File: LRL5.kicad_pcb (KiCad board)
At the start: 2 copper layers, 150 x 50 mm, 38 parts, among them J1 POWER, J2 On/Off, J5 OUT, J6 MODE, J7 ADJUST, Q1 BC549, U1 BA033CC0T, U2 NHD-C0220BIZ

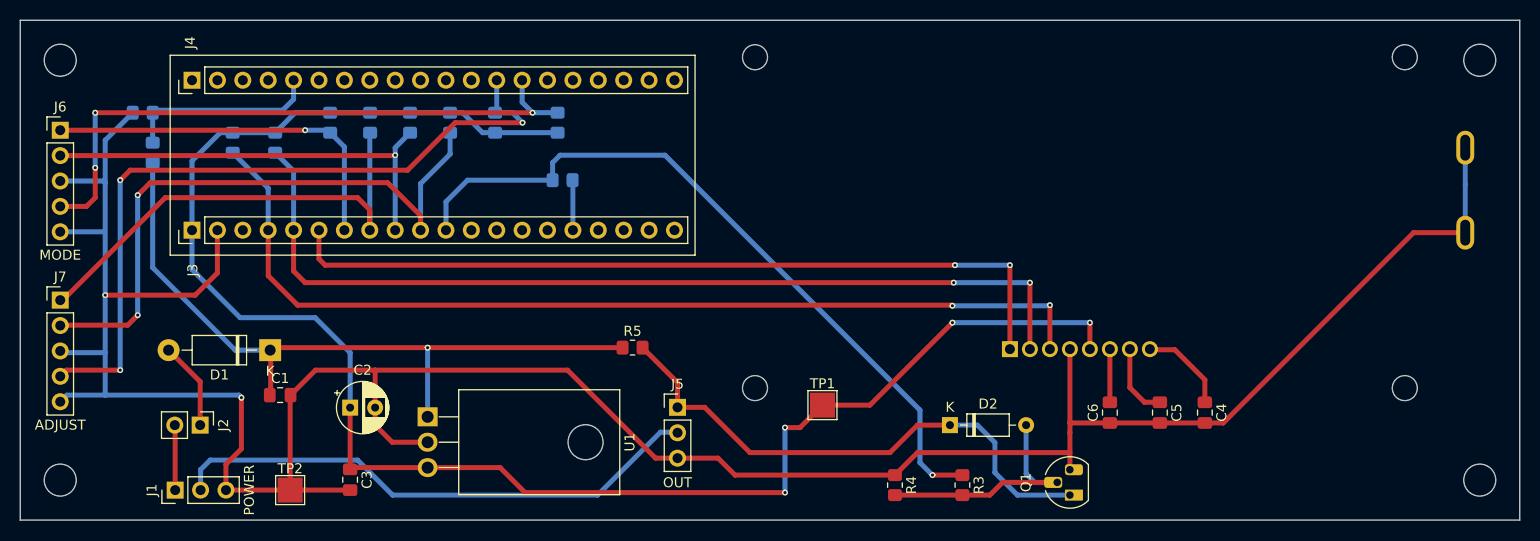
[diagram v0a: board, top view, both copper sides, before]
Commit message: Fix some silkscreen overlaps
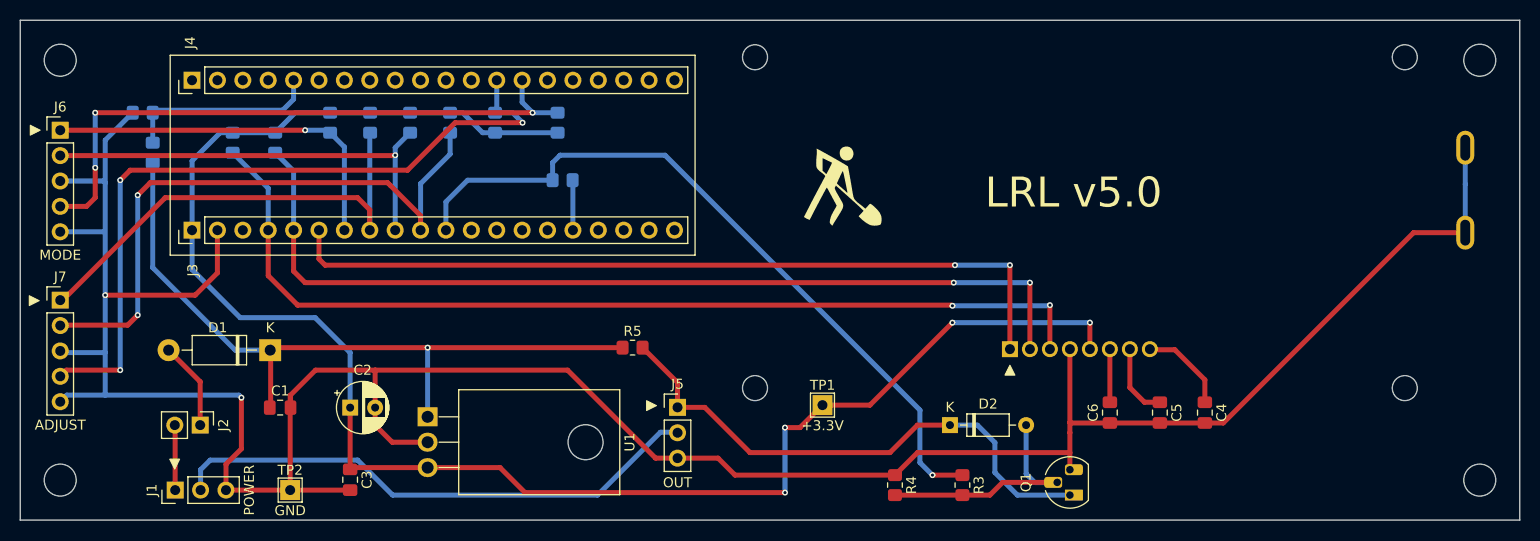
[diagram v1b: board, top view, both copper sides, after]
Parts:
- added G***: LOGO, LOGO, F.Cu at (202.0, 46.5)
- H1, H2, H3, H4: value MountingHole -> (none)
- TP1, TP2: footprint TestPoint:TestPoint_Pad_2.5x2.5mm -> TestPoint:TestPoint_THTPad_2.0x2.0mm_Drill1.0mm
- moved C1 1.25 mm to (146.0, 68.8)
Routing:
- net +BATT: track 72.4 -> 73.7 mm
- net GND: track 273.8 -> 275.1 mm
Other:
- board text added: "LRL v5.0"

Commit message: Added filled zone
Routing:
- added copper zone on B.Cu, net GND
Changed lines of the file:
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@@
 		(net 41)
 	)
+	(zone
+		(net 2)
+		(net_name "GND")
+		(layer "B.Cu")
+		(name "FZ")
+		(hatch edge 0.5)
+		(connect_pads
+			(clearance 0.5)
+		)
+		(min_thickness 0.25)
+		(filled_areas_thickness no)
+		(fill yes
+			(thermal_gap 0.5)
+			(thermal_bridge_width 0.5)
+			(island_removal_mode 1)
+			(island_area_min 10)
+		)
+		(polygon
+			(pts
+				(xy 120.5 30.5) (xy 269.5 30.5) (xy 269.5 79.5) (xy 120.5 79.5)
+			)
+		)
+	)
 )

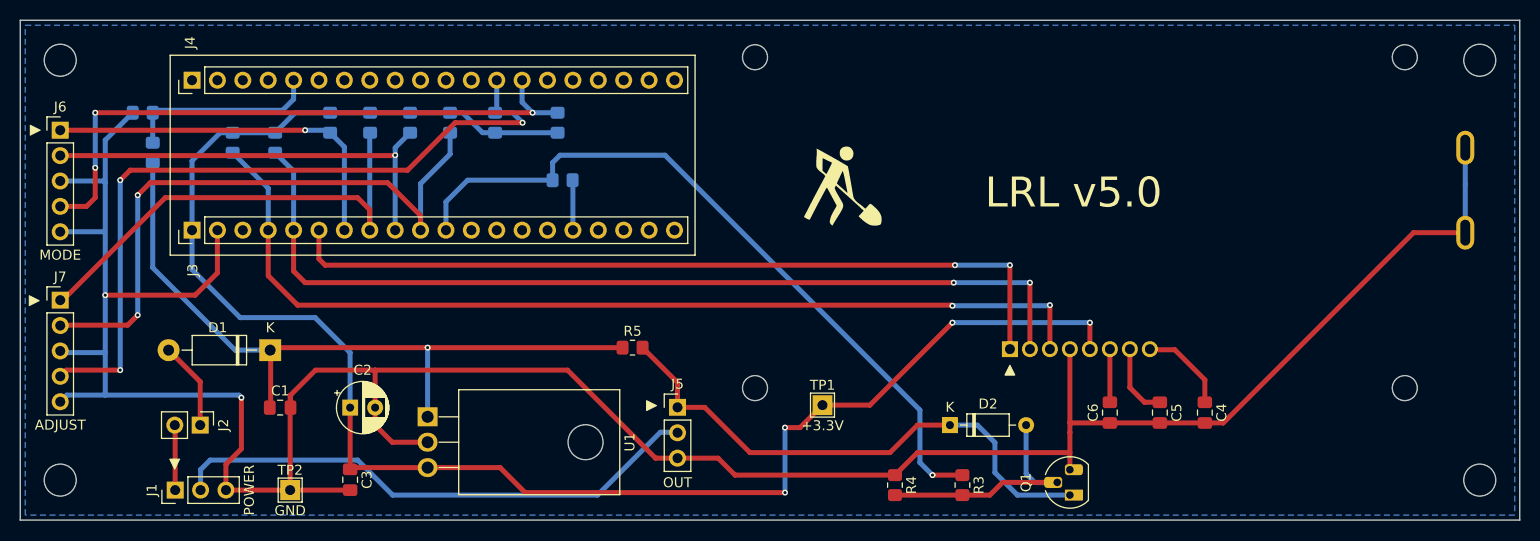
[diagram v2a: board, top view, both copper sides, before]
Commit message: Fix fill zone clearing
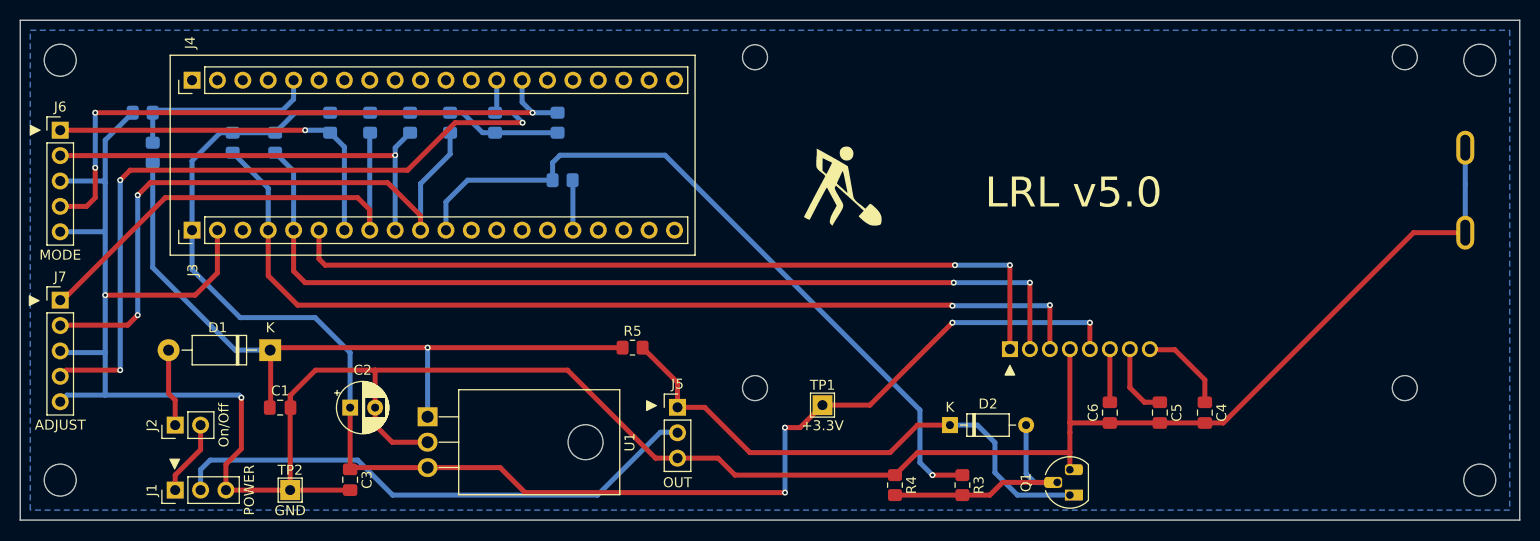
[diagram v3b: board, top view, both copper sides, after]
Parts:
- moved J2 2.50 mm to (135.5, 70.5), turned to 90 degrees
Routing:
- net Net-(J1-Pin_1): track 6.52 -> 7.56 mm
- net Net-(D1-A): track 8.81 -> 7.82 mm
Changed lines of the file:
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@@
 	(footprint "Connector_PinHeader_2.54mm:PinHeader_1x02_P2.54mm_Vertical"
 		(layer "F.Cu")
-		(at 138 70.5 -90)
+		(at 135.5 70.5 90)
 		(descr "Through hole straight pin header, 1x02, 2.54mm pitch, single row")
 		(tags "Through hole pin header THT 1x02 2.54mm single row")
@@
 		(property "Value" "On/Off"
 			(at 0 4.87 90)
-			(layer "F.Fab")
+			(layer "F.SilkS")
 			(effects
 				(font
@@
 		)
 		(property "Footprint" "Connector_PinHeader_2.54mm:PinHeader_1x02_P2.54mm_Vertical"
-			(at 0 0 -90)
+			(at 0 0 90)
 			(unlocked yes)
 			(layer "F.Fab")
@@
 		)
 		(property "Datasheet" ""
-			(at 0 0 -90)
+			(at 0 0 90)
 			(unlocked yes)
 			(layer "F.Fab")
@@
 		)
 		(property "Description" "Generic connector, single row, 01x02, script generated (kicad-library-utils/schlib/autogen/connector/)"
-			(at 0 0 -90)
+			(at 0 0 90)
 			(unlocked yes)
 			(layer "F.Fab")
@@
 		(attr through_hole)
 		(fp_line
-			(start -1.33 3.87)
-			(end 1.33 3.87)
+			(start -1.33 -1.33)
+			(end 0 -1.33)
 			(stroke
 				(width 0.12)
@@
 		)
 		(fp_line
-			(start -1.33 1.27)
-			(end -1.33 3.87)
+			(start -1.33 0)
+			(end -1.33 -1.33)
 			(stroke
 				(width 0.12)
@@
 		)
 		(fp_line
-			(start -1.33 1.27)
-			(end 1.33 1.27)
+			(start 1.33 1.27)
+			(end 1.33 3.87)
 			(stroke
 				(width 0.12)
@@
 		)
 		(fp_line
-			(start 1.33 1.27)
-			(end 1.33 3.87)
+			(start -1.33 1.27)
+			(end 1.33 1.27)
 			(stroke
 				(width 0.12)
@@
 		)
 		(fp_line
-			(start -1.33 0)
-			(end -1.33 -1.33)
+			(start -1.33 1.27)
+			(end -1.33 3.87)
 			(stroke
 				(width 0.12)
@@
 		)
 		(fp_line
-			(start -1.33 -1.33)
-			(end 0 -1.33)
+			(start -1.33 3.87)
+			(end 1.33 3.87)
 			(stroke
 				(width 0.12)
@@
 		)
 		(fp_line
-			(start -1.8 4.35)
-			(end 1.8 4.35)
+			(start 1.8 -1.8)
+			(end -1.8 -1.8)
 			(stroke
 				(width 0.05)
@@
 		)
 		(fp_line
-			(start 1.8 4.35)
-			(end 1.8 -1.8)
+			(start -1.8 -1.8)
+			(end -1.8 4.35)
 			(stroke
 				(width 0.05)
@@
 		)
 		(fp_line
-			(start -1.8 -1.8)
-			(end -1.8 4.35)
+			(start 1.8 4.35)
+			(end 1.8 -1.8)
 			(stroke
 				(width 0.05)
@@
 		)
 		(fp_line
-			(start 1.8 -1.8)
-			(end -1.8 -1.8)
+			(start -1.8 4.35)
+			(end 1.8 4.35)
 			(stroke
 				(width 0.05)
@@
 		)
 		(fp_line
-			(start -1.27 3.81)
-			(end -1.27 -0.635)
+			(start 1.27 -1.27)
+			(end 1.27 3.81)
 			(stroke
 				(width 0.1)
@@
 		)
 		(fp_line
-			(start 1.27 3.81)
-			(end -1.27 3.81)
+			(start -0.635 -1.27)
+			(end 1.27 -1.27)
 			(stroke
 				(width 0.1)
@@
 		)
 		(fp_line
-			(start -0.635 -1.27)
-			(end 1.27 -1.27)
+			(start 1.27 3.81)
+			(end -1.27 3.81)
 			(stroke
 				(width 0.1)
@@
 		)
 		(fp_line
-			(start 1.27 -1.27)
-			(end 1.27 3.81)
+			(start -1.27 3.81)
+			(end -1.27 -0.635)
 			(stroke
 				(width 0.1)
@@
 		)
 		(fp_text user "${REFERENCE}"
-			(at 0 1.27 0)
+			(at 0 1.27 360)
 			(layer "F.Fab")
 			(effects
@@
 		)
 		(pad "1" thru_hole rect
-			(at 0 0 270)
+			(at 0 0 90)
 			(size 1.7 1.7)
 			(drill 1)
@@
 		)
 		(pad "2" thru_hole oval
-			(at 0 2.54 270)
+			(at 0 2.54 90)
 			(size 1.7 1.7)
 			(drill 1)
@@
 		(fp_arc
 			(start -34.75 -19.8)
-			(mid -32.458355 -22.049621)
+			(mid -32.458355 -22.049622)
 			(end -30.251542 -19.716724)
 			(stroke
@@
 	)
 	(segment
-		(start 138 70.5)
-		(end 138 66.16)
+		(start 134.84 63)
+		(end 134.84 67.34)
 		(width 0.5)
 		(layer "F.Cu")
@@
 	)
 	(segment
-		(start 138 66.16)
-		(end 134.84 63)
+		(start 135.495 70.535)
+		(end 135.46 70.5)
+		(width 0.5)
+		(layer "F.Cu")
+		(net 7)
+	)
+	(segment
+		(start 134.84 67.34)
+		(end 135.5 68)
+		(width 0.5)
+		(layer "F.Cu")
+		(net 7)
+	)
+	(segment
+		(start 135.5 68)
+		(end 135.5 70.5)
 		(width 0.5)
 		(layer "F.Cu")
@@
 	)
 	(segment
+		(start 138.04 72.96)
+		(end 135.5 75.5)
+		(width 0.5)
+		(layer "F.Cu")
+		(net 10)
+	)
+	(segment
 		(start 135.5 77)
 		(end 135.495 76.995)
@@
 	)
 	(segment
-		(start 135.495 76.995)
-		(end 135.495 70.535)
+		(start 138.04 70.5)
+		(end 138.04 72.96)
 		(width 0.5)
 		(layer "F.Cu")
@@
 	)
 	(segment
-		(start 135.495 70.535)
-		(end 135.46 70.5)
+		(start 135.5 75.5)
+		(end 135.5 77)
 		(width 0.5)
 		(layer "F.Cu")
@@
 		(hatch edge 0.5)
 		(connect_pads
-			(clearance 0.5)
+			(clearance 1)
 		)
 		(min_thickness 0.25)
@@
 			(thermal_gap 0.5)
 			(thermal_bridge_width 0.5)
-			(island_removal_mode 1)
-			(island_area_min 10)
 		)
 		(polygon
 			(pts
-				(xy 120.5 30.5) (xy 269.5 30.5) (xy 269.5 79.5) (xy 120.5 79.5)
+				(xy 121 31) (xy 269 31) (xy 269 79) (xy 121 79)
 			)
 		)

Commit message: Some PCB optimizations 1
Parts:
- removed R10, R11, R12, R13, R14, R9: 10k, Resistor_SMD:R_0805_2012Metric_Pad1.20x1.40mm_HandSolder
- H1, H2, H3, H4: value (none) -> MountingHole
- moved R6 15.0 mm to (150.2, 56.5), turned to 90 degrees
- moved R7 14.3 mm to (142.5, 56.5), turned to 90 degrees
- moved R8 10.2 mm to (174.2, 56.2)
- moved R5 3.51 mm to (184.8, 63.0)
- moved J2 2.55 mm to (133.0, 71.0)
- moved U1 1.92 mm to (160.8, 67.8)
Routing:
- net +3.3V: track 169.8 -> 130.5 mm, vias 4 -> 3
- net ADJUST_B: track 62.8 -> 51.8 mm
- net ADJUST_A: track 47.5 -> 37.7 mm
- net I2C1_SDA: track 97.6 -> 90.8 mm
- net FOUT: track 73.8 -> 67.3 mm
- net I2C1_SCL: track 93.4 -> 87.5 mm
- net ADJUST_SW1: track 74.1 -> 68.7 mm, vias 3 -> 2
- net MODE_B: track 43.9 -> 41.0 mm
- net +BATT: track 73.7 -> 76.5 mm, vias 1 -> 0
- net Net-(D2-K): track 55.1 -> 53.4 mm
- net MODE_SW1: track 62.4 -> 60.7 mm, vias 3 -> 2
- net Net-(J1-Pin_1): track 7.56 -> 6.02 mm
- net BATT/2: track 54.0 -> 52.9 mm
- net Net-(D1-A): track 7.82 -> 8.76 mm
- net GND: track 275.1 -> 275.9 mm
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- removed copper zone on B.Cu, net GND
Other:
- board text added: "+3.3V"
- board text added: "ADJUST_A"
- board text added: "ADJUST_B"
- board text added: "ADJUST_SW1"
- board text added: "FIN"
- board text added: "FOUT"
- board text added: "GND"
- board text added: "I2C1_SDA"
- board text added: "I2C_SCL"
- board text added: "MODE_A"
- board text added: "MODE_B"
- board text added: "MODE_SW1"
- board text added: "VBAT"

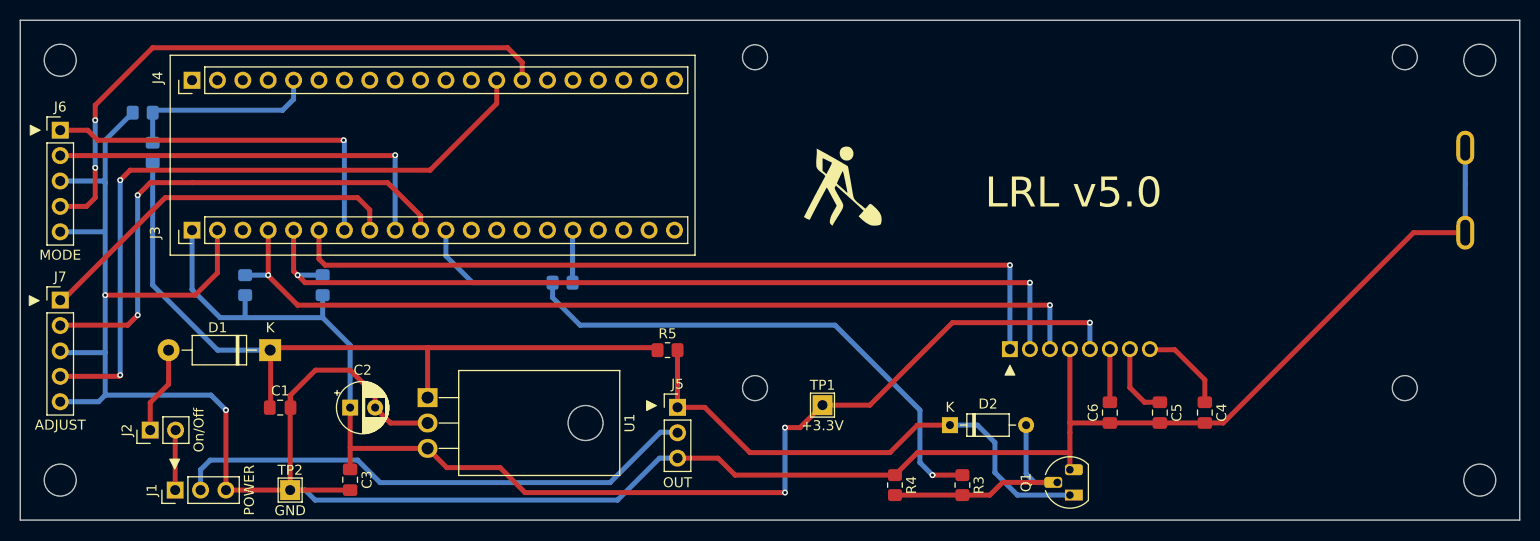
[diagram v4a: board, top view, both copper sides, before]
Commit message: Redesign board for smaller size
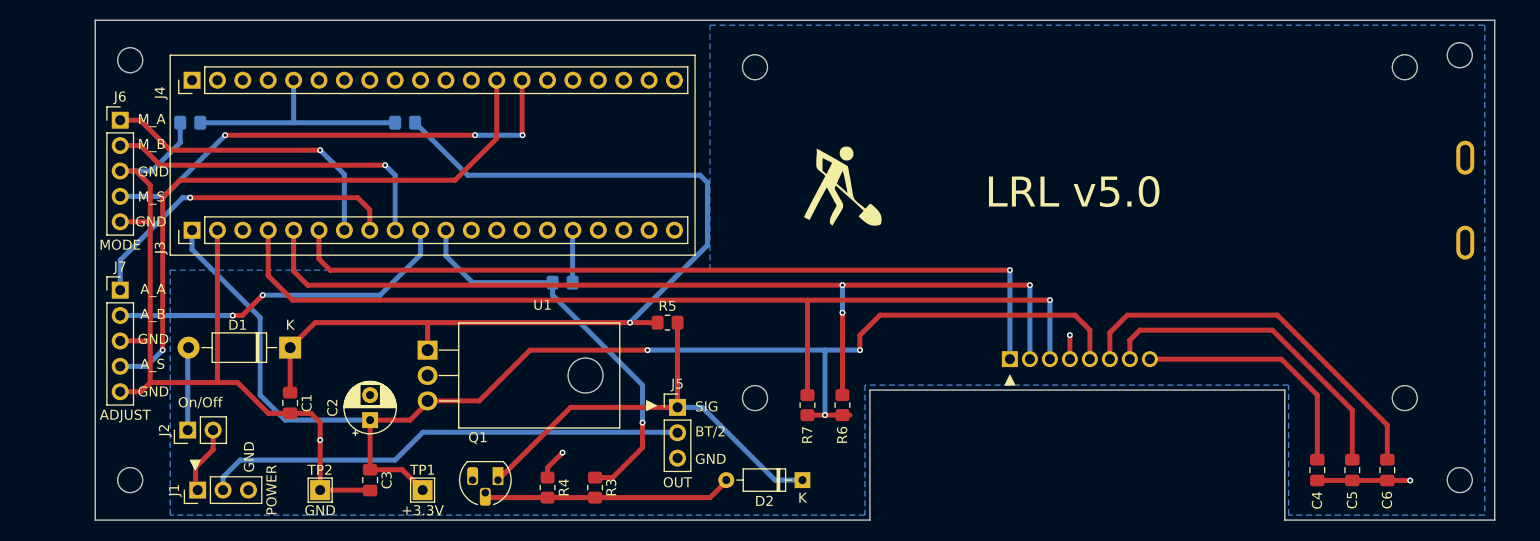
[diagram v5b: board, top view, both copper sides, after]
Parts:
- H1, H2, H3, H4: value MountingHole -> Hole; footprint MountingHole:MountingHole_3.2mm_M3 -> MountingHole:MountingHole_2.5mm
- R6, R7: moved to F.Cu
- moved R7 57.5 mm to (198.8, 68.5)
- moved Q1 57.2 mm to (167.8, 76.0), turned to 180 degrees
- moved R6 53.4 mm to (202.2, 68.5)
- moved TP1 40.9 mm to (160.2, 77.0)
- moved R3 36.8 mm to (177.5, 76.8)
- moved R4 34.8 mm to (172.8, 76.8)
- moved C6 28.3 mm to (256.8, 75.0)
- moved R1 25.4 mm to (158.5, 40.2), turned to 180 degrees
- moved C5 20.1 mm to (253.2, 75.0)
- moved D2 15.7 mm to (198.2, 76.0), turned to 180 degrees
- moved C4 12.6 mm to (249.8, 75.0)
- moved H1 7.00 mm to (131.0, 34.0)
- moved H3 7.00 mm to (131.0, 76.0)
- moved J6 6.08 mm to (130.0, 40.0)
- moved J7 6.08 mm to (130.0, 57.0)
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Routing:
- net GND: track 275.9 -> 103.7 mm, vias 2 -> 4
- net Net-(U2-VOUT): track 5.31 -> 39.1 mm
- net FOUT: track 67.3 -> 40.6 mm
- net Net-(U2-C1+): track 7.46 -> 32.8 mm
- net +BATT: track 76.5 -> 93.7 mm, vias 0 -> 1
- net ADJUST_B: track 51.8 -> 35.0 mm
- net Net-(U2-C1-): track 9.62 -> 24.7 mm
- net MODE_SW1: track 60.7 -> 48.4 mm, vias 2 -> 3
- net I2C1_SCL: track 87.5 -> 96.8 mm, vias 2 -> 3
- net I2C1_SDA: track 90.8 -> 99.2 mm, vias 2 -> 1
- net Net-(D2-K): track 53.4 -> 45.0 mm
- net MODE_A: track 37.8 -> 30.2 mm
- net ADJUST_SW1: track 68.7 -> 61.9 mm, vias 2 -> 1
- net MODE_B: track 41.0 -> 34.2 mm
- net ADJUST_A: track 37.7 -> 33.1 mm, vias 0 -> 1
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- added copper zone on B.Cu, net GND
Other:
- board size 150 x 50 mm -> 140 x 50 mm
- board text added: "A_A"
- board text added: "A_B"
- board text added: "A_S"
- board text added: "BT/2"
- board text added: "M_A"
- board text added: "M_B"
- board text added: "M_S"
- board text added: "SIG"

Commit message: Some optimizations 2
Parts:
- moved C6 32.4 mm to (229.0, 58.2), turned to -90 degrees
- moved C5 26.7 mm to (232.5, 58.2), turned to 90 degrees
- moved C4 21.6 mm to (236.0, 58.3), turned to 90 degrees
- moved R1 11.3 mm to (147.2, 41.2), turned to 90 degrees
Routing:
- net Net-(U2-VOUT): track 39.1 -> 4.61 mm
- net Net-(U2-C1+): track 32.8 -> 5.23 mm
- net Net-(U2-C1-): track 24.7 -> 5.82 mm
- net VBAT: track 23.9 -> 13.8 mm
- net +BATT: track 93.7 -> 83.8 mm, vias 1 -> 0
- net ADJUST_A: track 33.1 -> 35.3 mm
- net MODE_A: track 30.2 -> 31.9 mm
- net ADJUST_B: track 35.0 -> 36.5 mm
- net ADJUST_SW1: track 61.9 -> 62.9 mm, vias 1 -> 2
- net MODE_SW1: track 48.4 -> 47.4 mm, vias 3 -> 1
- net MODE_B: track 34.2 -> 35.1 mm

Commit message: Change diodes footprints
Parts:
- D1: footprint Diode_THT:D_DO-41_SOD81_P10.16mm_Horizontal -> Diode_SMD:D_SMA_Handsoldering
- D2: footprint Diode_THT:D_DO-35_SOD27_P7.62mm_Horizontal -> Diode_SMD:D_SMA_Handsoldering
- moved D1 6.75 mm to (140.2, 62.8)
- moved D2 2.00 mm to (196.2, 76.0)
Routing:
- net +BATT: track 83.8 -> 88.1 mm, vias 0 -> 1
- net Net-(D2-A): track 25.1 -> 28.2 mm
- net Net-(D2-K): track 45.0 -> 46.6 mm
- net GND: track 103.9 -> 105.1 mm
- net ADJUST_B: track 36.5 -> 37.5 mm
- net Net-(D1-A): track 8.29 -> 8.66 mm, vias 0 -> 1
